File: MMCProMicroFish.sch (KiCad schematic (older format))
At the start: 24 parts, among them J1 USB2_C_Receptacle, J2 Conn_01x12, J3 Conn_01x12, J4 Conn_01x05, U1 ATmega32U4-AU, X1 Resonator

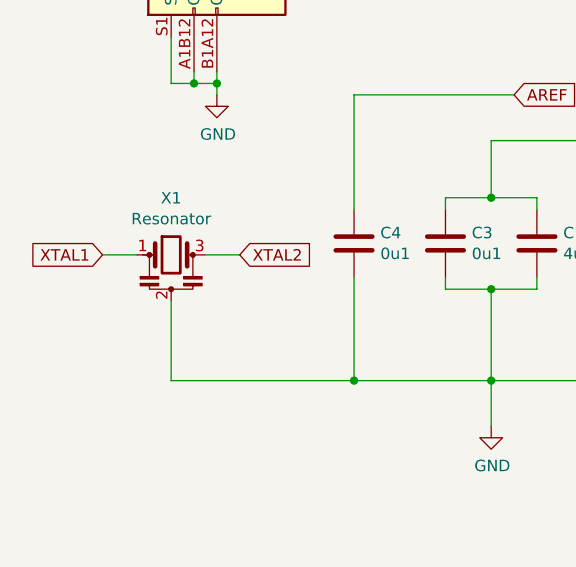
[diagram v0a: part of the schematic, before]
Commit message: Rerouted
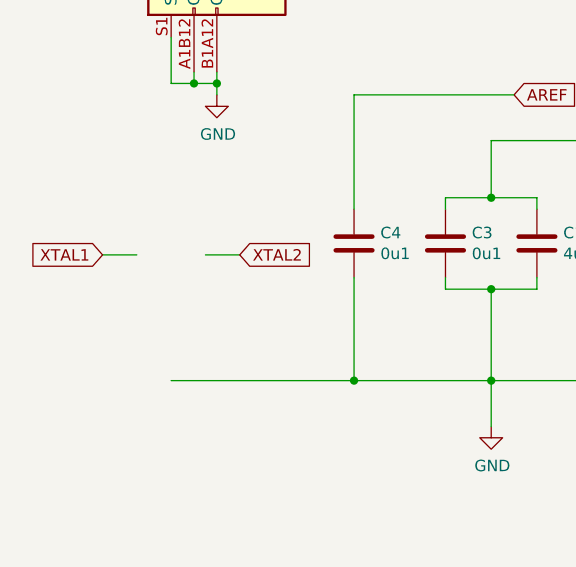
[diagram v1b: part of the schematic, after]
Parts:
- removed X1: Resonator, proj_local:Resonator_SMD_muRata_CSTxExxV-3Pin_3.0x1.1mm_HandSoldering_Compact, symbol Device:Resonator
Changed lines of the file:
@@
 	1900 2700 2600 2700
-Wire Wire Line
-	1100 3600 1100 3950
 Wire Wire Line
 	1100 3950 1900 3950
@@
 Wire Wire Line
 	4600 3800 4750 3800
-$Comp
-L Device:Resonator X1
-U 1 1 5B775AC8
-P 1100 3400
-F 0 "X1" H 1100 3648 50  0000 C CNN
-F 1 "Resonator" H 1100 3557 50  0000 C CNN
-F 2 "proj_local:Resonator_SMD_muRata_CSTxExxV-3Pin_3.0x1.1mm_HandSoldering_Compact" H 1075 3400 50  0001 C CNN
-F 3 "~" H 1075 3400 50  0001 C CNN
-	1    1100 3400
-	1    0    0    -1
-$EndComp
 Wire Wire Line
 	1250 3400 1400 3400
